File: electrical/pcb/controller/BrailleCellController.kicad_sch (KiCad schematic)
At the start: 3 parts, among them J1 Conn_01x08_Socket, J2 Conn_01x08_Socket, U1 HV509K6-G

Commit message: Power System
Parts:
- added J3, J4: Conn_01x04_Socket, symbol Connector:Conn_01x04_Socket
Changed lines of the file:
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@@
+	)
+	(symbol
+		(lib_id "Connector:Conn_01x04_Socket")
+		(at 146.05 106.68 0)
+		(unit 1)
+		(exclude_from_sim no)
+		(in_bom yes)
+		(on_board yes)
+		(dnp no)
+		(fields_autoplaced yes)
+		(property "Reference" "J3"
+			(at 147.32 106.6799 0)
+			(effects
+				(font
+					(size 1.27 1.27)
+				)
+				(justify left)
+			)
+		)
+		(property "Value" "Conn_01x04_Socket"
+			(at 147.32 109.2199 0)
+			(effects
+				(font
+					(size 1.27 1.27)
+				)
+				(justify left)
+			)
+		)
+		(property "Footprint" ""
+			(at 146.05 106.68 0)
+			(effects
+				(font
+					(size 1.27 1.27)
+				)
+				(hide yes)
+			)
+		)
+		(property "Datasheet" "~"
+			(at 146.05 106.68 0)
+			(effects
+				(font
+					(size 1.27 1.27)
+				)
+				(hide yes)
+			)
+		)
+		(property "Description" "Generic connector, single row, 01x04, script generated"
+			(at 146.05 106.68 0)
+			(effects
+				(font
+					(size 1.27 1.27)
+				)
+				(hide yes)
+			)
+		)
+		(pin "4"
+		)
+		(pin "2"
+		)
+		(pin "3"
+		)
+		(pin "1"
+		)
+		(instances
+			(project ""
+				(path "/a0053d15-3fe6-4047-92ee-091d4acfd1a5"
+					(reference "J3")
+					(unit 1)
+				)
+			)
+		)
+	)
+	(symbol
+		(lib_id "Connector:Conn_01x04_Socket")
+		(at 146.05 119.38 0)
+		(unit 1)
+		(exclude_from_sim no)
+		(in_bom yes)
+		(on_board yes)
+		(dnp no)
+		(fields_autoplaced yes)
+		(property "Reference" "J4"
+			(at 147.32 119.3799 0)
+			(effects
+				(font
+					(size 1.27 1.27)
+				)
+				(justify left)
+			)
+		)
+		(property "Value" "Conn_01x04_Socket"
+			(at 147.32 121.9199 0)
+			(effects
+				(font
+					(size 1.27 1.27)
+				)
+				(justify left)
+			)
+		)
+		(property "Footprint" ""
+			(at 146.05 119.38 0)
+			(effects
+				(font
+					(size 1.27 1.27)
+				)
+				(hide yes)
+			)
+		)
+		(property "Datasheet" "~"
+			(at 146.05 119.38 0)
+			(effects
+				(font
+					(size 1.27 1.27)
+				)
+				(hide yes)
+			)
+		)
+		(property "Description" "Generic connector, single row, 01x04, script generated"
+			(at 146.05 119.38 0)
+			(effects
+				(font
+					(size 1.27 1.27)
+				)
+				(hide yes)
+			)
+		)
+		(pin "4"
+		)
+		(pin "2"
+		)
+		(pin "3"
+		)
+		(pin "1"
+		)
+		(instances
+			(project "BrailleCellController"
+				(path "/a0053d15-3fe6-4047-92ee-091d4acfd1a5"
+					(reference "J4")
+					(unit 1)
+				)
+			)
+		)
 	)
 	(symbol

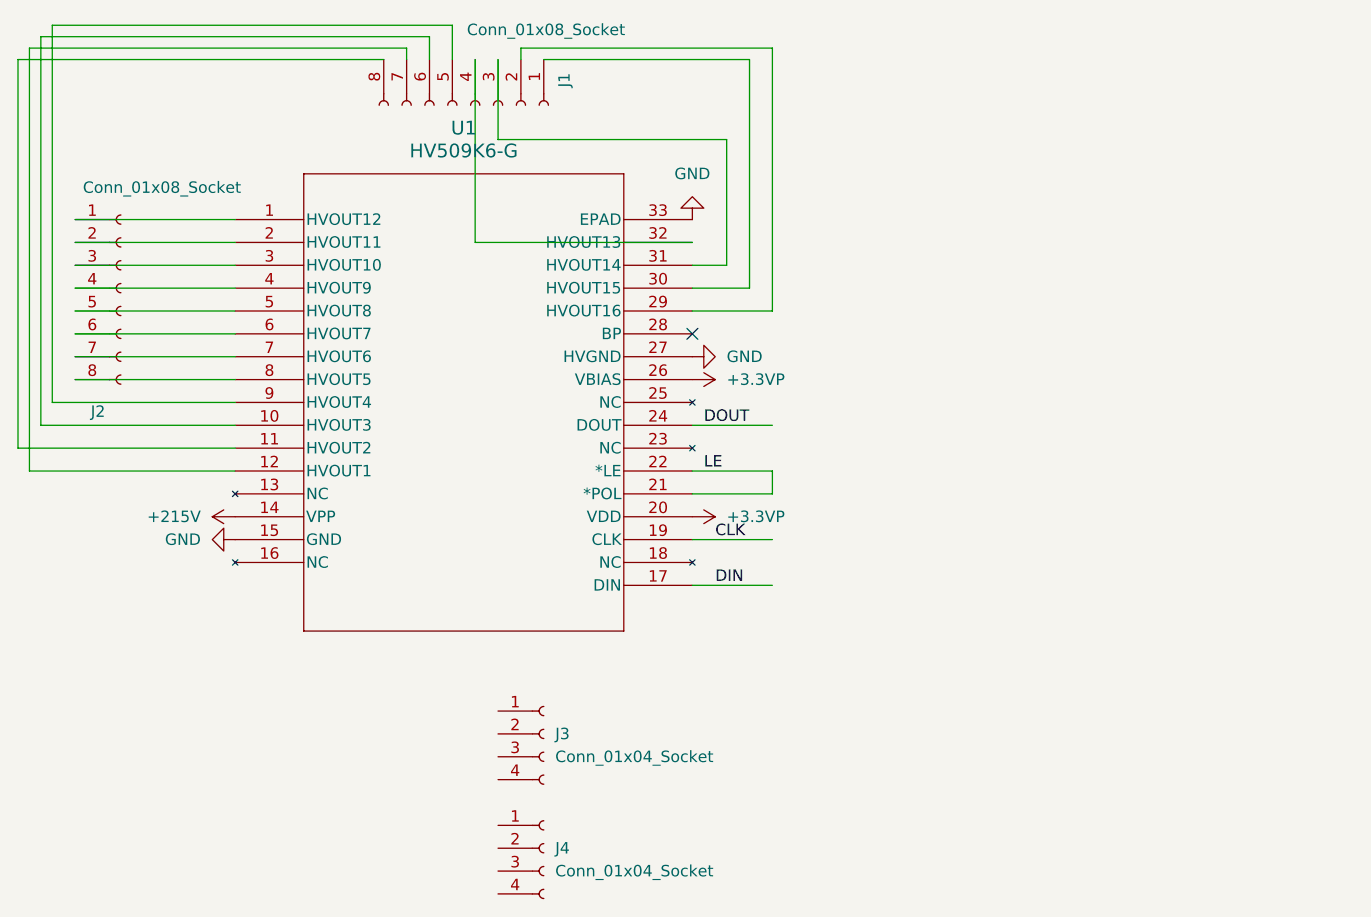
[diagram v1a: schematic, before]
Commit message: cell shifter routed
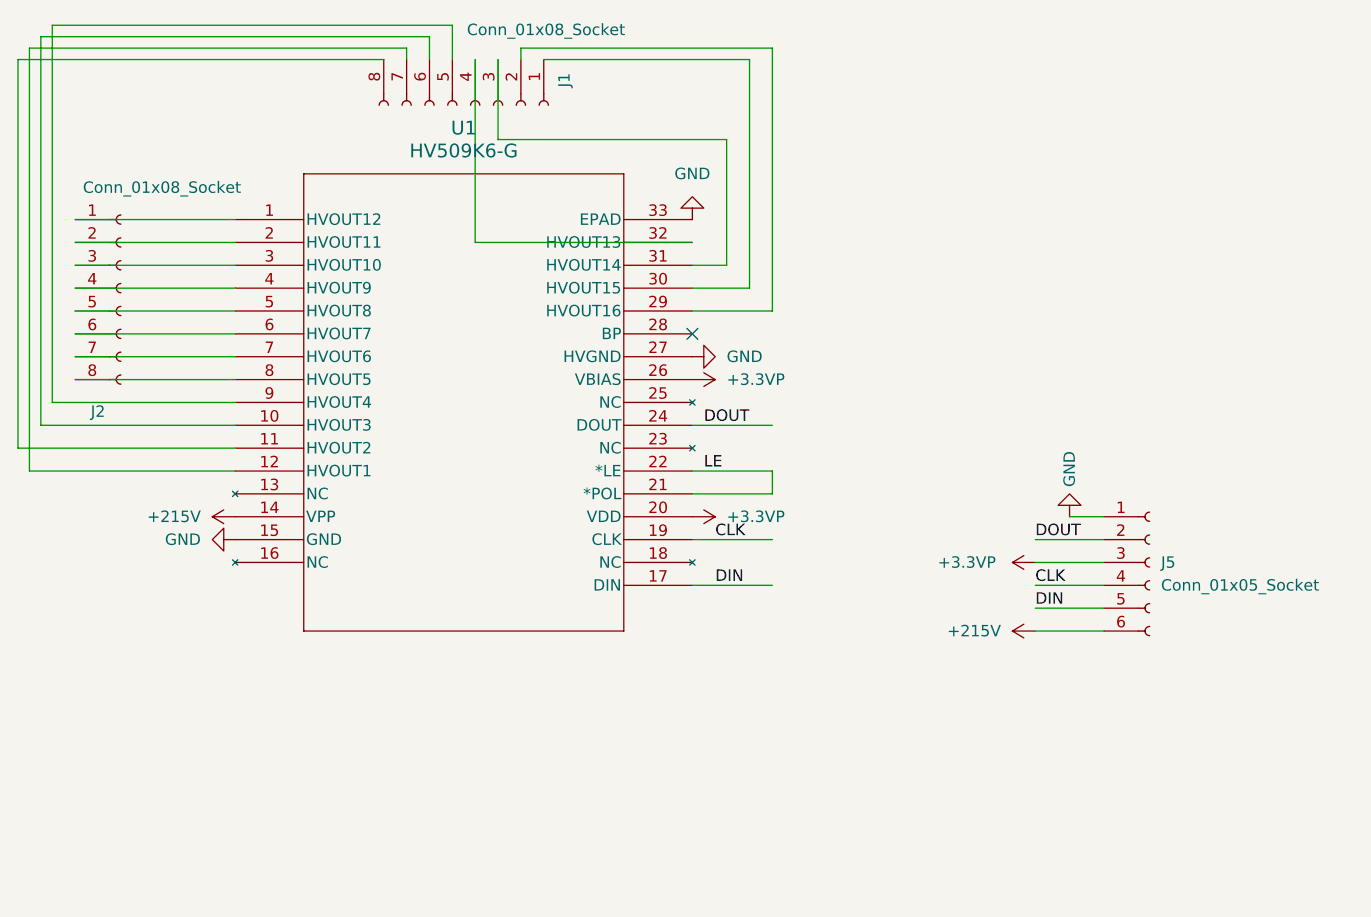
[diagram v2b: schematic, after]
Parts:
- removed J3, J4: Conn_01x04_Socket, symbol Connector:Conn_01x04_Socket
- added J5: Conn_01x05_Socket, Connector_PinHeader_1.00mm:PinHeader_1x06_P1.00mm_Vertical, symbol Connector:Conn_01x06_Socket
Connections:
- net +215V: now also J5.6 (Pin_6)
- net +3.3VP: now also J5.3 (Pin_3)
- net CLK: now also J5.4 (Pin_4)
- net DIN: now also J5.5 (Pin_5)
- net DOUT: now also J5.2 (Pin_2)
- net GND: now also J5.1 (Pin_1)
